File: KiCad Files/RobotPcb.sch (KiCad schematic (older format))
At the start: 22 parts, among them IC1 LM2576, IC2 LM2576, IC3 L293D, IC4 L293D, J1 Screw_Terminal_01x02, J2 Screw_Terminal_01x02, J3 Screw_Terminal_01x02, J4 Screw_Terminal_01x02

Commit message: PCB Files added
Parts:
- removed C1: 100μF, symbol C
- removed D1, D2: (no value), symbol DIODE
- removed JP1, JP2, JP3, JP4: PINHD-1X3, symbol PINHD-1X3
- removed MS1: FEATHERWING, symbol FEATHERWING
- added C1: 100μF, Capacitors_THT:CP_Radial_D6.3mm_P2.50mm, symbol CP1
- added D1, D2: SCHOTTKY-DIODE, Diodes_THT:D_DO-201AD_P12.70mm_Horizontal, symbol SCHOTTKY-DIODE
- added J10, J11, J8, J9: Conn_01x03_Male, Pin_Headers:Pin_Header_Straight_1x03_Pitch2.54mm, symbol Conn_01x03_Male
- added J5: Screw_Terminal_01x02, Connectors_Terminal_Blocks:TerminalBlock_Altech_AK300-2_P5.00mm, symbol Screw_Terminal_01x02
- added J6, J7: Conn_01x16_Female, Socket_Strips:Socket_Strip_Straight_1x16_Pitch2.54mm, symbol Conn_01x16_Female
- added R3: 3.00k, Resistors_THT:R_Axial_DIN0207_L6.3mm_D2.5mm_P7.62mm_Horizontal, symbol R
- added R4: 1k, Resistors_THT:R_Axial_DIN0207_L6.3mm_D2.5mm_P7.62mm_Horizontal, symbol R
- C2: footprint (none) -> Capacitors_THT:CP_Radial_D6.3mm_P2.50mm
- C3: value 100μF -> 1000μF; footprint (none) -> Capacitors_THT:CP_Radial_D6.3mm_P2.50mm
- IC1, IC2: footprint (none) -> Custom:TO-220-5
- IC3, IC4: footprint DIL16 -> Housings_DIP:DIP-16_W7.62mm_Socket
- J1, J2, J3, J4: footprint (none) -> Connectors_Terminal_Blocks:TerminalBlock_Altech_AK300-2_P5.00mm
- L1, L2: footprint (none) -> Inductors_THT:L_Toroid_Vertical_L19.1mm_W8.1mm_P7.10mm_Bourns_5700
- R1: value 4.22k -> 5.10k; footprint (none) -> Resistors_THT:R_Axial_DIN0207_L6.3mm_D2.5mm_P7.62mm_Horizontal
- R2: footprint (none) -> Resistors_THT:R_Axial_DIN0207_L6.3mm_D2.5mm_P7.62mm_Horizontal
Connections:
- net IC2_5V: now also J10.2 (Pin_2), J11.2 (Pin_2), J7.10 (Pin_10), J8.2 (Pin_2), J9.2 (Pin_2), R3.1; no longer IC2.4 (FB)
- net LEFT_BACKWARDS: now also J6.9 (Pin_9)
- net LEFT_FORWARD: now also J6.8 (Pin_8)
- net RIGHT_BACKWARDS: now also J7.8 (Pin_8)
- net RIGHT_FORWARD: now also J7.7 (Pin_7)
- net SERVO_1_PWM: now also J7.6 (Pin_6), J9.1 (Pin_1)
- net SERVO_2_PWM: now also J7.5 (Pin_5), J8.1 (Pin_1)
- net SERVO_3_PWM: now also J11.1 (Pin_1), J7.4 (Pin_4)
- net SERVO_4_PWM: now also J10.1 (Pin_1), J7.3 (Pin_3)
- net WHEEL_EN: now also J7.9 (Pin_9)
- net MC_3.3V: now reaches IC3.8 (VCC2)
- net MC_3.3V: now also IC4.8 (VCC2), J6.15 (Pin_15)
- net at IC1.2 (OUT), L1.1: now also D2.1
- net at IC2.2 (OUT), L2.1: now also D1.1
- net +VDC renamed GND
- net GND: now also C1.2, D1.2, D2.2, J10.3 (Pin_3), J11.3 (Pin_3), J5.2 (Pin_2), J6.13 (Pin_13), J8.3 (Pin_3), J9.3 (Pin_3), R4.2; no longer IC1.1 (VIN), IC2.1 (VIN)
- new net: C1.1, IC1.1 (VIN), IC2.1 (VIN), J5.1 (Pin_1)
- new net: IC2.4 (FB), R3.2, R4.1
- no-connect marks 19 -> 20
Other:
- moved on the sheet: R2

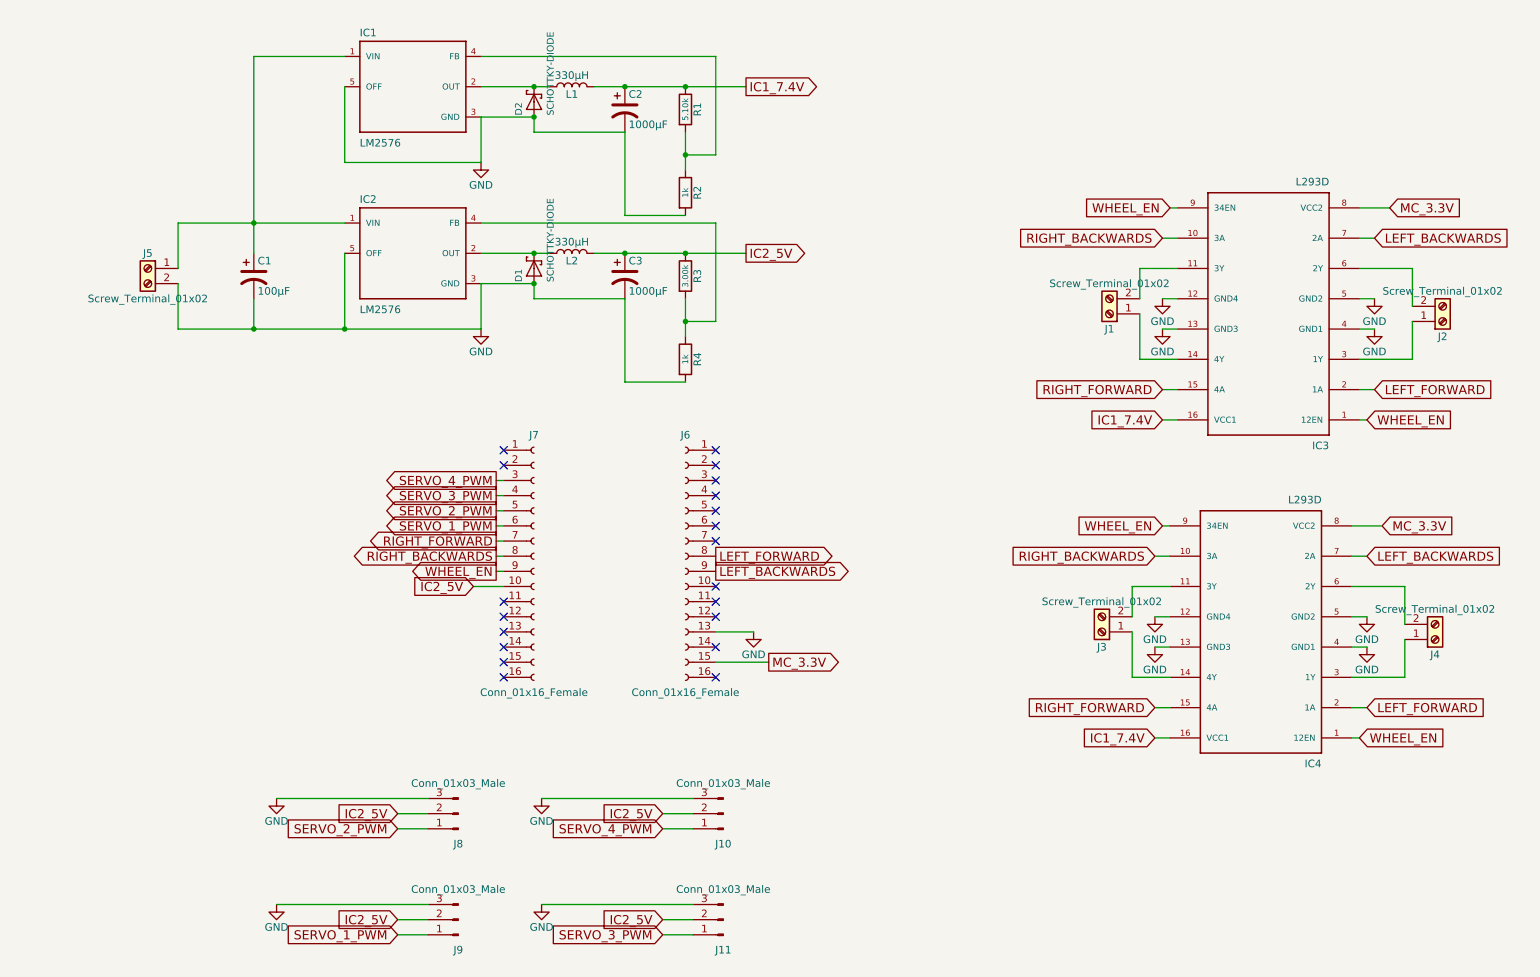
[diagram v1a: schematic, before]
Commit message: Fixed PCBs
PCB v1.1

Added schematic PDF, updated pinout for PCB
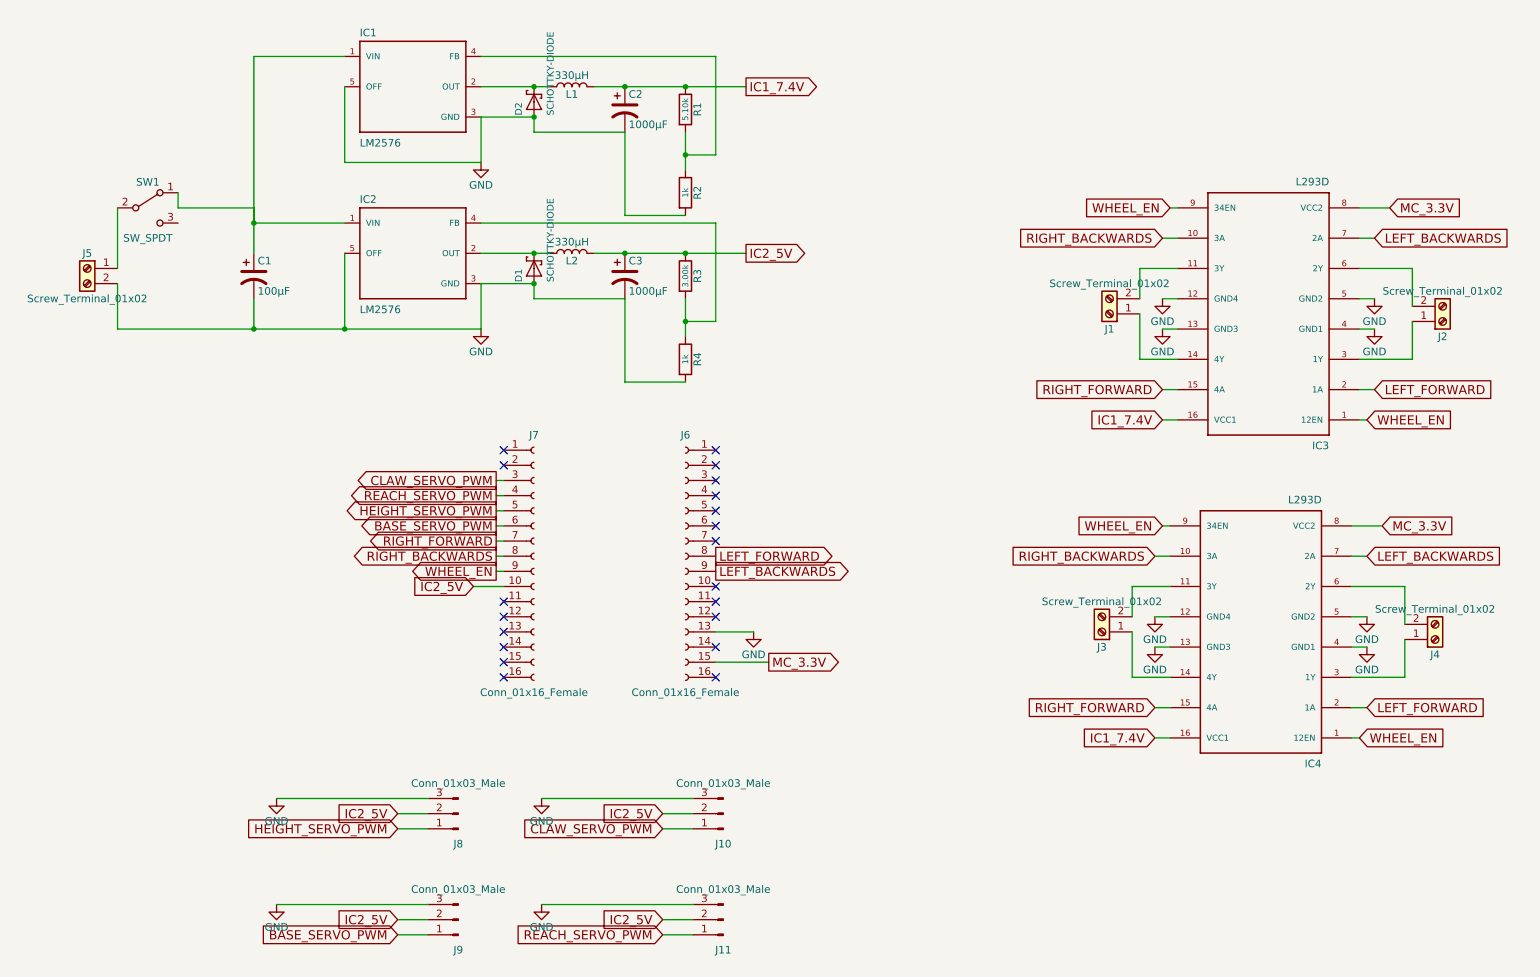
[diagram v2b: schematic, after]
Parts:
- added SW1: SW_SPDT, Custom footprints:L102021ML04Q_SPDT, symbol SW_SPDT
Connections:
- net at C1.1, IC1.1 (VIN), IC2.1 (VIN): now also SW1.1 (A); no longer J5.1 (Pin_1)
- net SERVO_1_PWM renamed BASE_SERVO_PWM
- net SERVO_2_PWM renamed HEIGHT_SERVO_PWM
- net SERVO_3_PWM renamed REACH_SERVO_PWM
- net SERVO_4_PWM renamed CLAW_SERVO_PWM
- new net: J5.1 (Pin_1), SW1.2 (B)
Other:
- moved on the sheet: J5
